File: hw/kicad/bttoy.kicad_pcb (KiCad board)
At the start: 2 copper layers, 41.9 x 44.4 mm, 35 parts, among them J1 USB-micro-b, J2 HC-07_BLUETOOTH, J3 ARM_10PIN, P1 +9V_DBG, P2 M1+, P3 M1-, P4 M2+, P5 M2-, SW1 SPDT (Apem MHSS1105), U1 AAT3221/MIC5504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

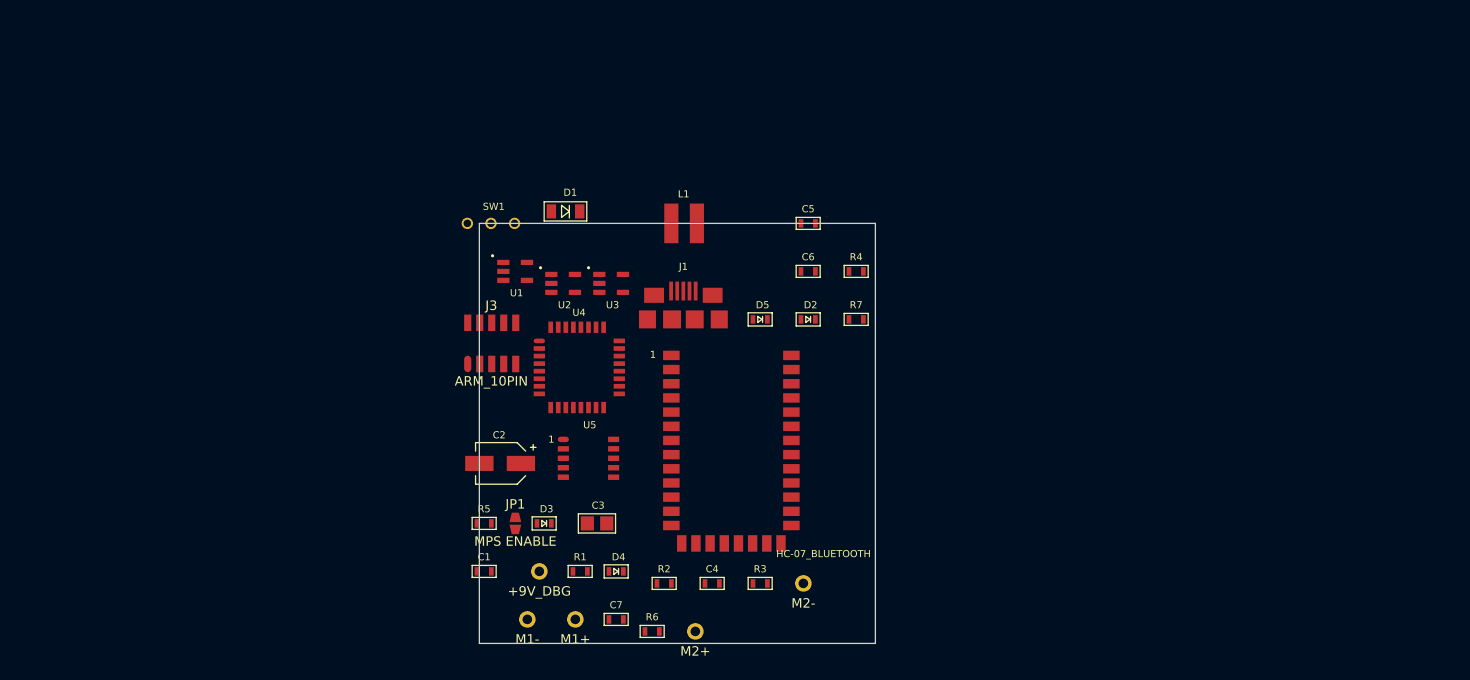
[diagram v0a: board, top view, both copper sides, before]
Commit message: - add bom, add acc. connections, reload parts on pcb
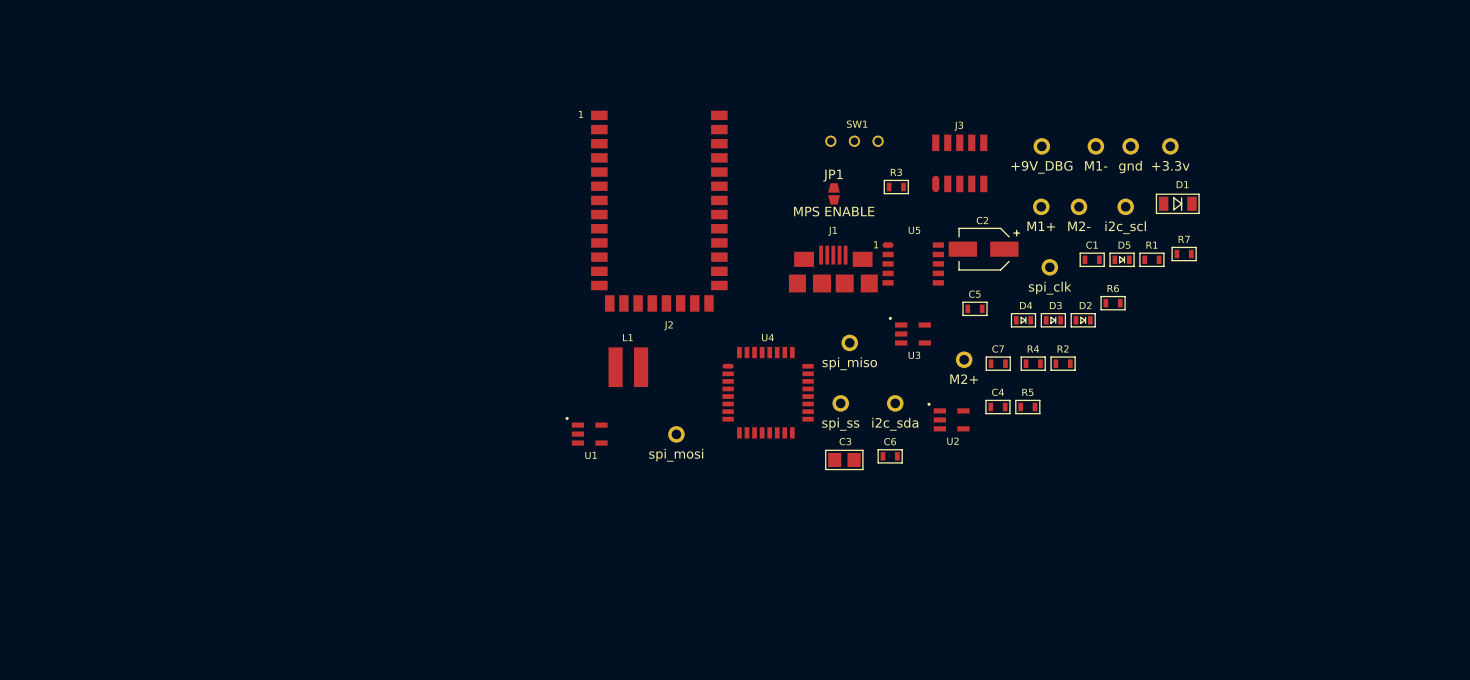
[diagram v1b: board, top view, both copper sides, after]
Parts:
- added P10: M1+, kicadlib:TEST_0.100, F.Cu at (192.8, 87.1)
- added P11: M1-, kicadlib:TEST_0.100, F.Cu at (198.6, 80.7)
- added P12: M2+, kicadlib:TEST_0.100, F.Cu at (184.7, 103.3)
- added P13: M2-, kicadlib:TEST_0.100, F.Cu at (196.8, 87.1)
- added P6: spi_mosi, kicadlib:TEST_0.100, F.Cu at (154.2, 111.2)
- added P7: spi_clk, kicadlib:TEST_0.100, F.Cu at (193.7, 93.5)
- added P8: +3.3v, kicadlib:TEST_0.100, F.Cu at (206.5, 80.7)
- added P9: gnd, kicadlib:TEST_0.100, F.Cu at (202.3, 80.7)
- P2: value M1+ -> i2c_sda
- P3: value M1- -> i2c_scl
- P4: value M2+ -> spi_ss
- P5: value M2- -> spi_miso
- moved P3 76.9 mm to (201.7, 87.1)
- moved C1 72.3 mm to (199.0, 92.8)
- moved P1 69.6 mm to (192.9, 80.7)
- moved R1 68.9 mm to (205.3, 92.8)
- moved D1 64.8 mm to (205.8, 86.8)
- moved R6 59.9 mm to (201.2, 97.3)
- moved R5 58.8 mm to (192.2, 108.3)
- moved D3 58.0 mm to (194.9, 99.2)
- moved C2 56.0 mm to (184.5, 91.6)
- moved J3 53.1 mm to (184.2, 82.5)
- moved D4 50.6 mm to (191.7, 99.2)
- moved C7 48.7 mm to (189.0, 103.7)
- moved JP1 48.5 mm to (170.9, 85.8)
- moved R2 48.2 mm to (195.9, 103.7)
- moved R3 44.4 mm to (178.2, 85.1)
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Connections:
- net Net-(U4-Pad10) renamed /acc_spi_miso
- P2 pad 1: /motor_1_+ -> /i2c_sda
- P3 pad 1: /motor_1_- -> /i2c_scl
- P4 pad 1: /motor_2_+ -> /spi_ss
- P5 pad 1: /motor_2_- -> /spi_miso
- U4 pad 11: Net-(U4-Pad11) -> /motor_2_B
- U4 pad 12: Net-(U4-Pad12) -> /motor_2_A
- U4 pad 13: /bt_rx -> /motor_1_B
- U4 pad 14: /bt_tx -> /motor_1_A
- U4 pad 15: Net-(U4-Pad15) -> /spi_mosi
- U4 pad 16: Net-(U4-Pad16) -> /spi_sclk
- U4 pad 23: Net-(U4-Pad23) -> /bt_tx
- U4 pad 24: Net-(U4-Pad24) -> /bt_rx
- U4 pad 7: Net-(U4-Pad7) -> /i2c_scl
- U4 pad 8: Net-(U4-Pad8) -> /i2c_sda
- U4 pad 9: Net-(U4-Pad9) -> /spi_ss
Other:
- board outline removed

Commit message: tune up schematic a bit more, and start positioning footprints on pcb
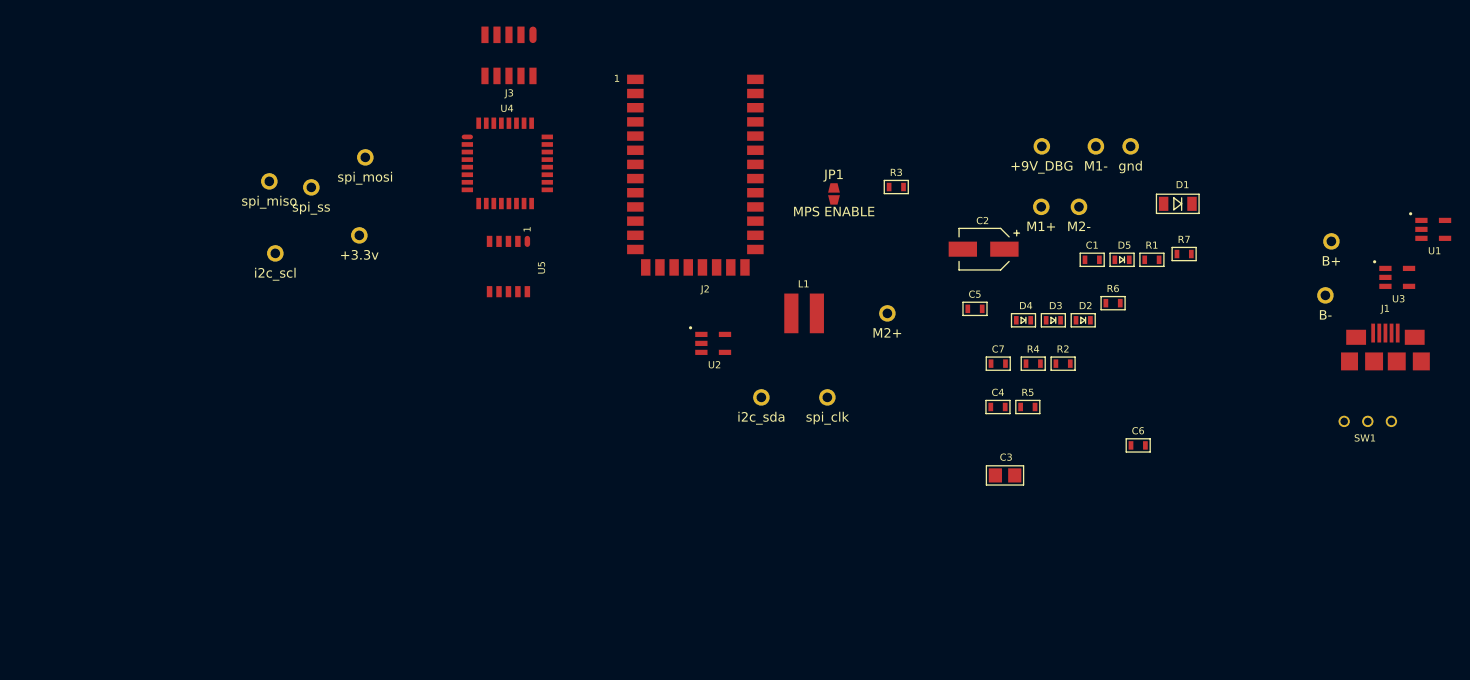
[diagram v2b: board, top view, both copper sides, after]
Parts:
- added P14: B-, kicadlib:TEST_0.100, F.Cu at (222.9, 96.5)
- added P15: B+, kicadlib:TEST_0.100, F.Cu at (223.5, 90.8)
- moved U1 91.9 mm to (233.0, 89.5)
- moved P3 90.1 mm to (111.8, 92.1)
- moved P8 86.3 mm to (120.7, 90.2)
- moved SW1 66.3 mm to (229.9, 109.9), turned to 180 degrees
- moved P5 63.8 mm to (111.1, 84.5)
- moved P4 60.5 mm to (115.6, 85.1)
- moved J1 59.0 mm to (229.2, 103.5)
- moved U3 51.6 mm to (229.2, 94.6)
- moved J3 49.0 mm to (136.5, 71.1), turned to 180 degrees
- moved P6 44.1 mm to (121.3, 81.9)
- moved U5 38.2 mm to (138.4, 90.8), turned to 270 degrees
- moved U4 36.7 mm to (132.1, 82.5)
- moved P7 27.3 mm to (170.2, 107.3)
- moved U2 26.5 mm to (156.8, 101.6)
- moved C6 26.3 mm to (203.8, 112.4)
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
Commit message: mps and dbg led's laid out
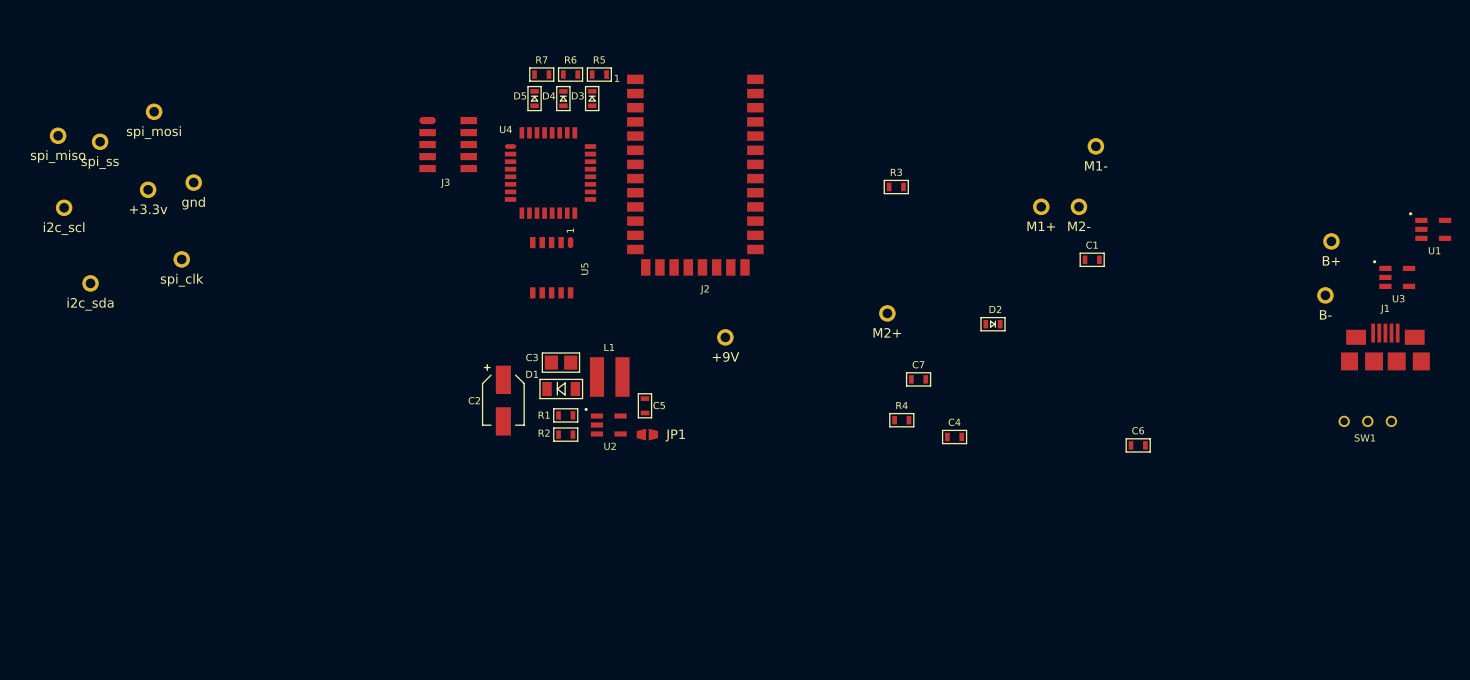
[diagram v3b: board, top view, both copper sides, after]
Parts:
- P1: value +9V_DBG -> +9V
- moved P9 99.2 mm to (103.1, 84.6)
- moved P2 72.0 mm to (92.2, 95.2)
- moved R7 70.6 mm to (140.7, 73.2)
- moved P7 69.9 mm to (101.9, 92.7)
- moved D5 65.4 mm to (139.2, 74.9), turned to 90 degrees
- moved D1 65.3 mm to (143.5, 106.4), turned to 180 degrees
- moved R1 64.2 mm to (143.3, 109.2)
- moved R6 62.3 mm to (143.8, 73.2)
- moved R5 57.4 mm to (146.8, 73.2)
- moved D3 55.2 mm to (145.3, 74.9), turned to 90 degrees
- moved D4 55.1 mm to (142.2, 74.9), turned to 90 degrees
- moved R2 54.7 mm to (141.7, 111.3), turned to 180 degrees
- moved C2 51.9 mm to (135.9, 109.9), turned to 90 degrees
- moved C3 48.5 mm to (141.0, 103.6)
- moved P1 39.1 mm to (159.4, 101.0)
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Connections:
- U4 pad 17: /dgb_led1 -> Net-(U4-Pad17)
- U4 pad 18: /dbg_led2 -> Net-(U4-Pad18)
- U4 pad 19: /dbg_led3 -> Net-(U4-Pad19)
- U4 pad 25: Net-(U4-Pad25) -> /dgb_led1
- U4 pad 26: Net-(U4-Pad26) -> /dbg_led2
- U4 pad 27: Net-(U4-Pad27) -> /dbg_led3

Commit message: arrange footprint groups in pcb, change position of power switch to control all batt output
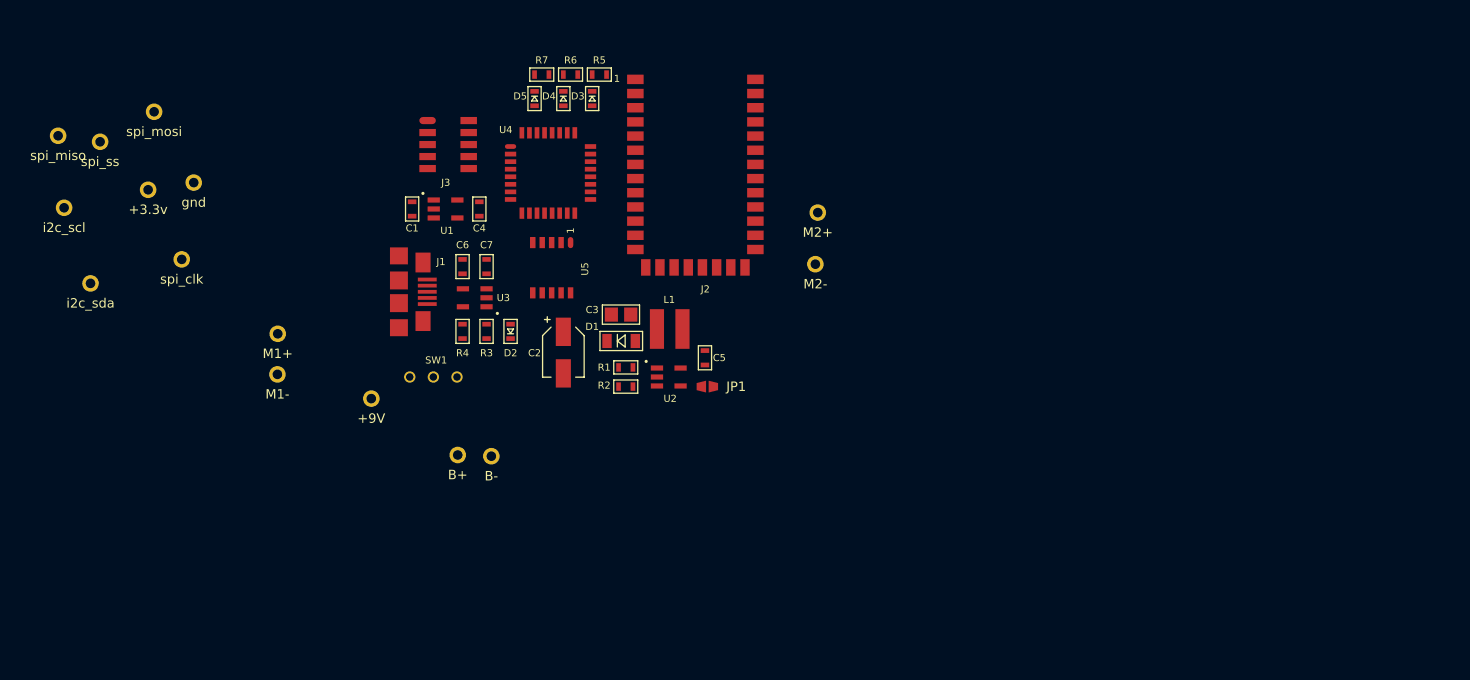
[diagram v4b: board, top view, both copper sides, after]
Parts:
- moved J1 104.7 mm to (124.8, 96.1), turned to 270 degrees
- moved U1 104.5 mm to (128.5, 87.4)
- moved SW1 104.0 mm to (126.0, 105.2), turned to 0 degrees
- moved P15 95.2 mm to (131.1, 113.4)
- moved U3 95.1 mm to (134.1, 96.8), turned to 180 degrees
- moved P11 89.9 mm to (112.0, 104.9)
- moved P14 89.9 mm to (134.6, 113.5)
- moved P10 81.9 mm to (112.0, 100.6)
- moved C6 74.9 mm to (131.6, 92.7), turned to 90 degrees
- moved C1 73.0 mm to (126.2, 86.6), turned to 90 degrees
- moved C4 56.1 mm to (133.3, 88.1), turned to 270 degrees
- moved D2 51.8 mm to (136.7, 101.1), turned to 270 degrees
- moved C7 48.2 mm to (134.1, 92.7), turned to 90 degrees
- moved R4 48.0 mm to (131.6, 101.1), turned to 270 degrees
- moved R3 46.5 mm to (134.1, 99.6), turned to 90 degrees
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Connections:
- C1 pad 1: /batt+ -> /vbatt_out
- C5 pad 1: /batt+ -> /vbatt_out
- C7 pad 1: Net-(C7-Pad1) -> /batt+
- L1 pad 2: /batt+ -> /vbatt_out
- SW1 pad 2: Net-(C7-Pad1) -> /batt+
- SW1 pad 3: /batt+ -> /vbatt_out
- U1 pad 1: /batt+ -> /vbatt_out
- U1 pad 3: /batt+ -> /vbatt_out
- U2 pad 5: /batt+ -> /vbatt_out
- U3 pad 3: Net-(C7-Pad1) -> /batt+
